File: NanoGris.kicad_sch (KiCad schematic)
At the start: 112 parts, among them J10 Conn_01x12, J11 Conn_01x12, J12 Conn_02x05_Odd_Even, J13 Conn_01x10, J14 Conn_01x10, J15 Conn_01x10, J16 Conn_01x03, J7 Conn_01x10, Q1 2N3904, Q2 2N3904, U1 MCP6002_1, U2 MCP6002_1, U3 MCP6002_1, U4 L7805, U5 LM4040LP-5, U6 74HC595, X1 CV_X, Y1 CV_Y

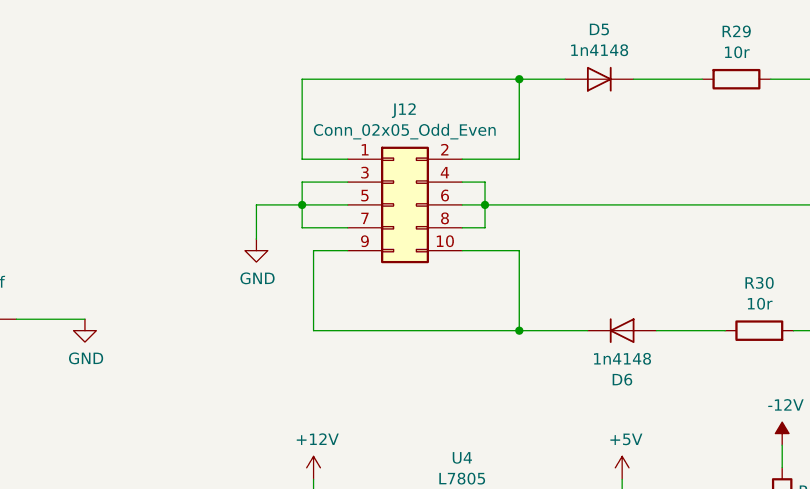
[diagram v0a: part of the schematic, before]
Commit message: Updated powerheader
Now with correct power schematic and boxed header.
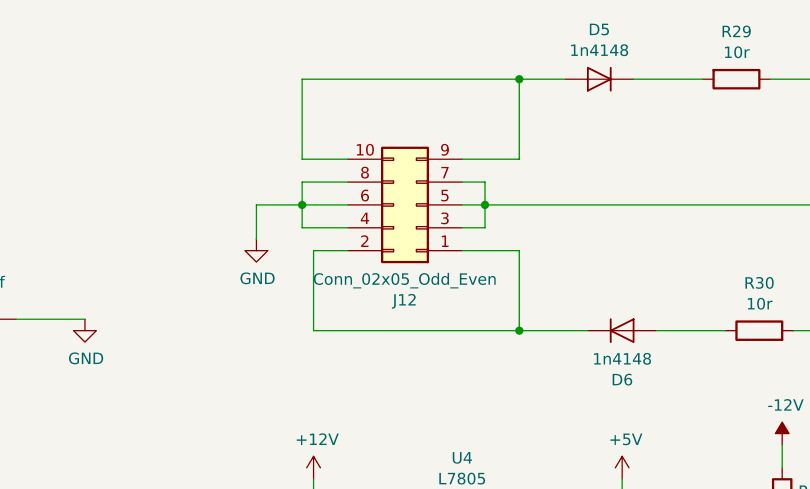
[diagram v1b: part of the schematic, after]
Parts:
- J12: footprint Connector_PinHeader_2.54mm:PinHeader_2x05_P2.54mm_Vertical -> Connector_IDC:IDC-Header_2x05_P2.54mm_Vertical
- P_CH1, P_CH2, P_CH3, P_RND1, P_TEMPO1, P_X1, P_Y1: footprint Potentiometer_THT:Potentiometer_Alps_RK09L_Single_Vertical -> Potentiometer_THT:Potentiometer_Alps_RK09K_Single_Vertical_round
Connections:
- net at J12.1 (Pin_1), J12.2 (Pin_2): now also D6.1 (K); no longer D5.2 (A)
- net at J12.10 (Pin_10), J12.9 (Pin_9): now also D5.2 (A); no longer D6.1 (K)
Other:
- moved on the sheet: J12
